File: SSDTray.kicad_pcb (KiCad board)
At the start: 2 copper layers, 216 x 80 mm, 22 parts, among them J1 SSD1, J10 SSD10, J11 SSD11, J12 SSD12, J13 SSD13, J14 SSD14, J15 SSD15, J16 SSD16, J17 SSD17, J18 SSD18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

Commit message: Remove autosave lock file and update active layer preset to 'All Layers'
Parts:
- turned J19 to 0 degrees
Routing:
- net /SSD3_TX+: track 0.00 -> 61.6 mm
- net /SSD3_TX-: track 0.00 -> 59.3 mm
- net /SSD1_TX-: track 0.00 -> 28.6 mm
- net /SSD1_TX+: track 0.00 -> 25.9 mm
- net /SSD2_TX-: track 0.00 -> 25.2 mm
- net /SSD2_TX+: track 0.00 -> 22.5 mm
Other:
- copper layers 2 -> 4

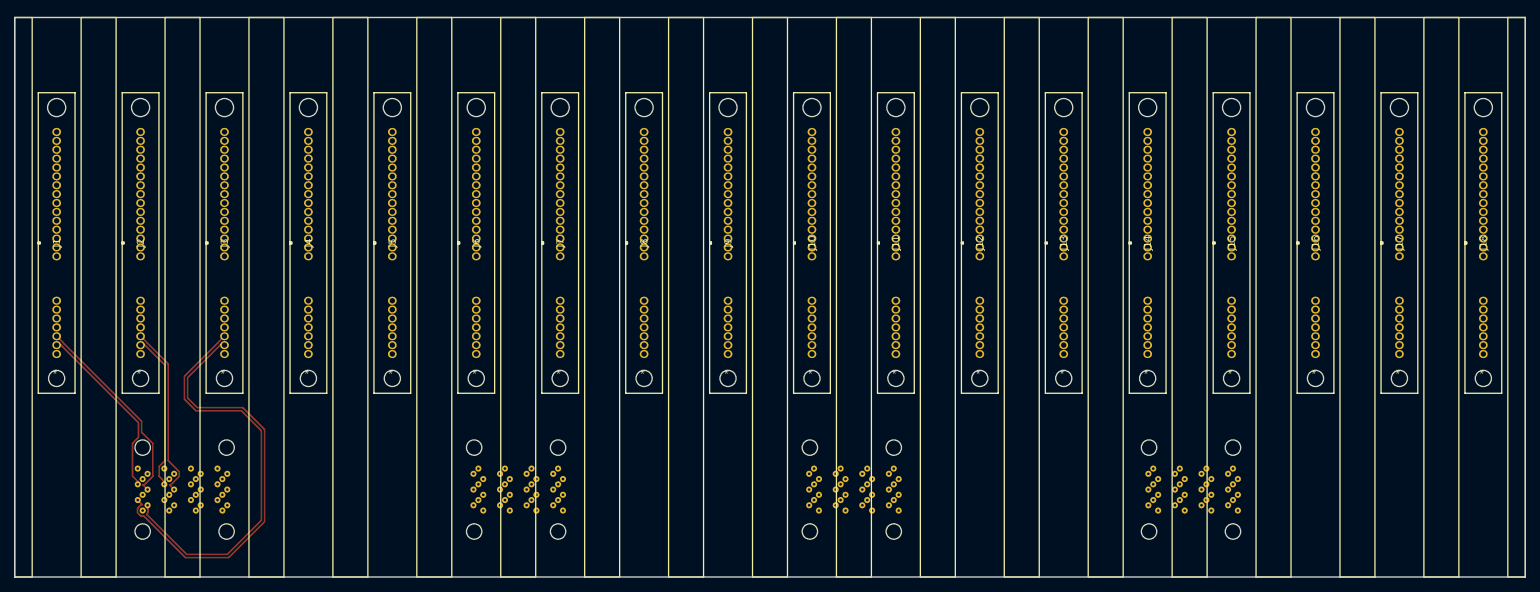
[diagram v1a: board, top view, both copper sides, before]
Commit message: Add Molex Connector footprint and symbol to libraries
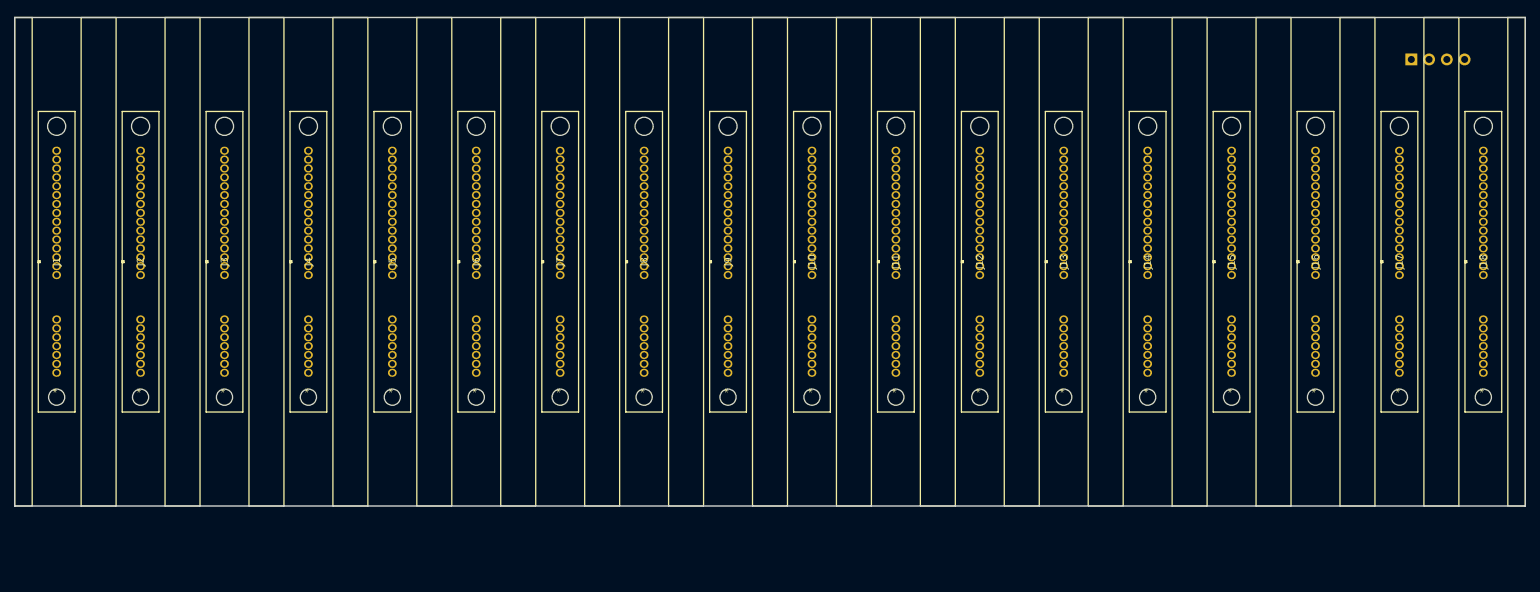
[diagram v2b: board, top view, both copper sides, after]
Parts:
- removed J19: SSD1-4, Mini SAS HD:TE_2227595-1
- removed J20: SSD5-8, Mini SAS HD:TE_2227595-1
- removed J21: SSD9-12, Mini SAS HD:TE_2227595-1
- removed J22: SSD13-16, Mini SAS HD:TE_2227595-1
- added J23: Conn_01x04, Connector_PinHeader_2.54mm:PinHeader_1x04_P2.54mm_Vertical, B.Cu at (227.7, 107.0)
- moved J1 2.68 mm to (34.0, 151.8)
- moved J10 2.68 mm to (142.0, 151.8)
- moved J11 2.68 mm to (154.0, 151.8)
- moved J12 2.68 mm to (166.0, 151.8)
- moved J13 2.68 mm to (178.0, 151.8)
- moved J14 2.68 mm to (190.0, 151.8)
- moved J15 2.68 mm to (202.0, 151.8)
- moved J16 2.68 mm to (214.0, 151.8)
- moved J17 2.68 mm to (226.0, 151.8)
- moved J18 2.68 mm to (238.0, 151.8)
- moved J2 2.68 mm to (46.0, 151.8)
- moved J3 2.68 mm to (58.0, 151.8)
- moved J4 2.68 mm to (70.0, 151.8)
- moved J5 2.68 mm to (82.0, 151.8)
- moved J6 2.68 mm to (94.0, 151.8)
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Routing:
- net /SSD3_TX+: track 61.6 -> 0.00 mm
- net /SSD3_TX-: track 59.3 -> 0.00 mm
- net /SSD1_TX-: track 28.6 -> 0.00 mm
- net /SSD1_TX+: track 25.9 -> 0.00 mm
- net /SSD2_TX-: track 25.2 -> 0.00 mm
- net /SSD2_TX+: track 22.5 -> 0.00 mm
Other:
- board size 216 x 80 mm -> 216 x 69.8 mm

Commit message: Add Mini SAS footprint and symbol to libraries; update design rules and dimensions in SSDTray.kicad_pro
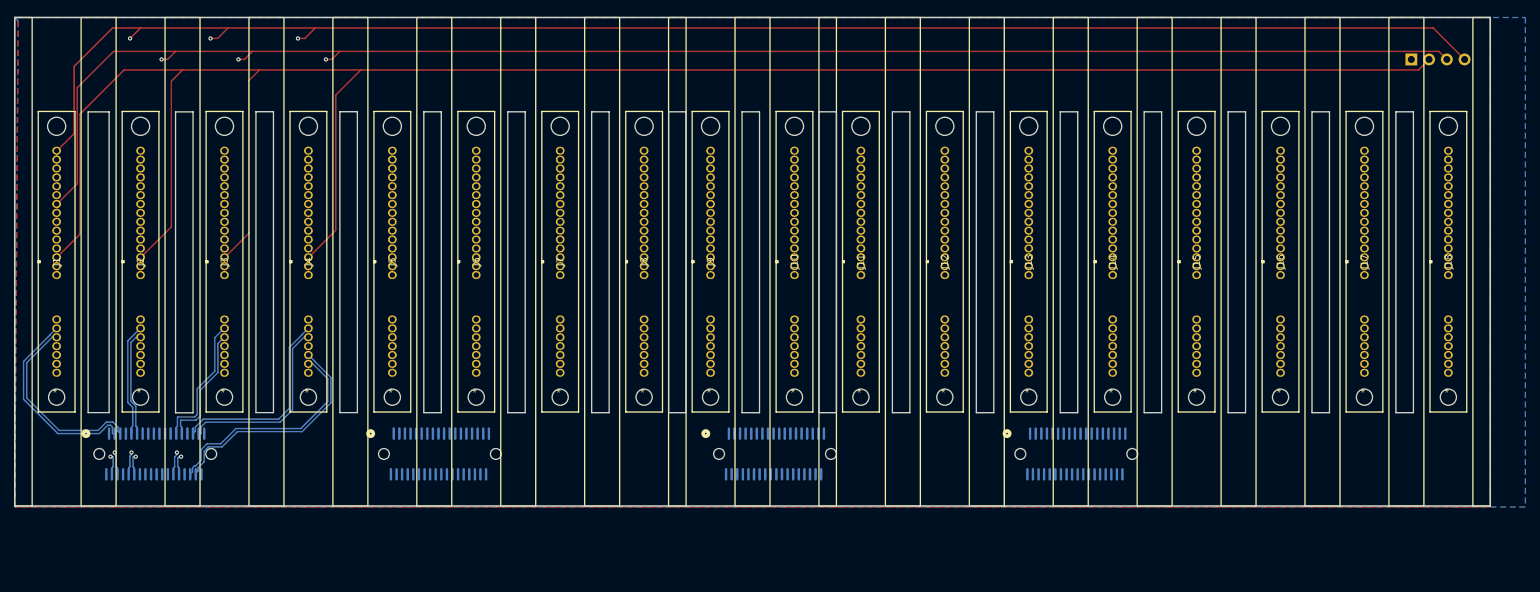
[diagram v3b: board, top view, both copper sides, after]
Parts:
- added J19: 1888020-4, Mini SAS:CONN36_1888020-4_TEC, B.Cu at (82.2, 160.5)
- added J20: 1888020-4, Mini SAS:CONN36_1888020-4_TEC, B.Cu at (41.5, 160.5)
- added J21: 1888020-4, Mini SAS:CONN36_1888020-4_TEC, B.Cu at (130.1, 160.5)
- added J22: 1888020-4, Mini SAS:CONN36_1888020-4_TEC, B.Cu at (173.2, 160.5)
- moved J11 5.00 mm to (149.0, 151.8)
- moved J12 5.00 mm to (161.0, 151.8)
- moved J13 5.00 mm to (173.0, 151.8)
- moved J14 5.00 mm to (185.0, 151.8)
- moved J15 5.00 mm to (197.0, 151.8)
- moved J16 5.00 mm to (209.0, 151.8)
- moved J17 5.00 mm to (221.0, 151.8)
- moved J18 5.00 mm to (233.0, 151.8)
- moved J10 2.50 mm to (139.5, 151.8)
- moved J9 2.50 mm to (127.5, 151.8)
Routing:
- net +3.3V: track 0.00 -> 318.8 mm
- net +5V: track 0.00 -> 299.1 mm, vias 0 -> 3
- net +12V: track 0.00 -> 284.9 mm, vias 0 -> 3
- net /SSD4_TX-: track 0.00 -> 33.0 mm
- net /SSD4_TX+: track 0.00 -> 32.1 mm
- net /SSD1_RX+: track 0.00 -> 28.7 mm
- net /SSD4_RX+: track 0.00 -> 28.2 mm
- net /SSD1_RX-: track 0.00 -> 27.7 mm
- net /SSD4_RX-: track 0.00 -> 27.1 mm
- net /SSD3_TX-: track 0.00 -> 21.9 mm, vias 0 -> 1
- net /SSD1_TX-: track 0.00 -> 20.8 mm, vias 0 -> 1
- net /SSD3_TX+: track 0.00 -> 20.7 mm, vias 0 -> 1
- net /SSD1_TX+: track 0.00 -> 19.6 mm, vias 0 -> 1
- net /SSD3_RX+: track 0.00 -> 19.4 mm
- net /SSD2_TX-: track 0.00 -> 19.3 mm, vias 0 -> 1
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- added copper zone on B.Cu, net GND
- added copper zone on F.Cu, net GND
- added copper zone on In2.Cu, net GND
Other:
- board size 216 x 69.8 mm -> 211 x 69.8 mm

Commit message: Limiting to 4 drives for testing
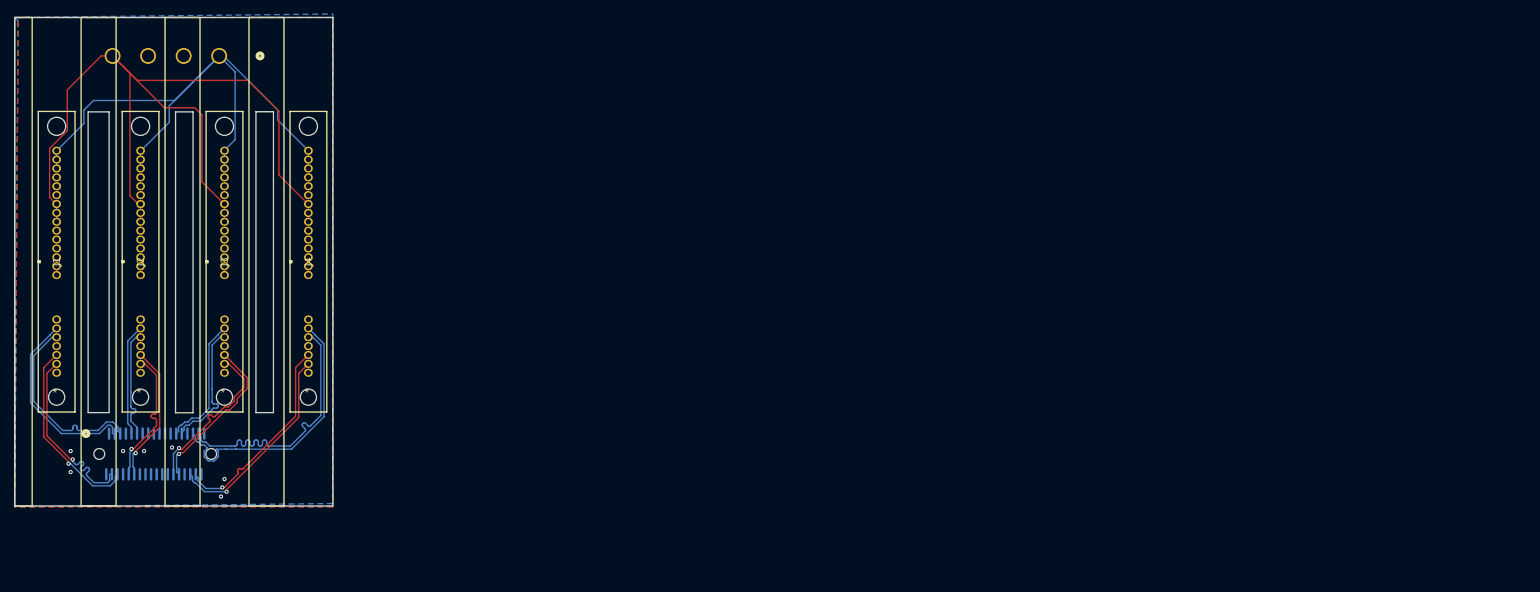
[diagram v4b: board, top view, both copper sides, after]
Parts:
- removed J10: SSD10, SSD Connector:CONN_877791001_MOL
- removed J11: SSD11, SSD Connector:CONN_877791001_MOL
- removed J12: SSD12, SSD Connector:CONN_877791001_MOL
- removed J13: SSD13, SSD Connector:CONN_877791001_MOL
- removed J14: SSD14, SSD Connector:CONN_877791001_MOL
- removed J15: SSD15, SSD Connector:CONN_877791001_MOL
- removed J16: SSD16, SSD Connector:CONN_877791001_MOL
- removed J17: SSD17, SSD Connector:CONN_877791001_MOL
- removed J18: SSD18, SSD Connector:CONN_877791001_MOL
- removed J19, J21, J22: 1888020-4, Mini SAS:CONN36_1888020-4_TEC
- removed J23: Conn_01x04, Connector_PinHeader_2.54mm:PinHeader_1x04_P2.54mm_Vertical
- removed the J5 at (82.0, 151.8)
- removed J6: SSD6, SSD Connector:CONN_877791001_MOL
- removed J7: SSD7, SSD Connector:CONN_877791001_MOL
- removed J8: SSD8, SSD Connector:CONN_877791001_MOL
- removed J9: SSD9, SSD Connector:CONN_877791001_MOL
- added U1: 350211-1, 4Pin ATX Molex:350211-1_TYC, B.Cu at (57.2, 106.5)
- renumbered J20 to J5
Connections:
- J1 pad P1: +3.3V -> unconnected-(J1-PadP1)
- J1 pad P2: +3.3V -> unconnected-(J1-PadP1)
- J1 pad P3: +3.3V -> unconnected-(J1-PadP1)
- J2 pad P1: +3.3V -> unconnected-(J2-PadP1)
- J2 pad P2: +3.3V -> unconnected-(J2-PadP1)
- J2 pad P3: +3.3V -> unconnected-(J2-PadP1)
- J3 pad P1: +3.3V -> unconnected-(J3-PadP1)
- J3 pad P2: +3.3V -> unconnected-(J3-PadP1)
- J3 pad P3: +3.3V -> unconnected-(J3-PadP1)
- J4 pad P1: +3.3V -> unconnected-(J4-PadP1)
- J4 pad P2: +3.3V -> unconnected-(J4-PadP1)
- J4 pad P3: +3.3V -> unconnected-(J4-PadP1)
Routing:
- net +3.3V: track 318.8 -> 0.00 mm
- net +12V: track 284.9 -> 92.7 mm, vias 3 -> 0
- net +5V: track 299.1 -> 129.8 mm, vias 3 -> 0
- net /SSD4_RX-: track 27.1 -> 39.1 mm
- net /SSD4_RX+: track 28.2 -> 39.3 mm
- net /SSD1_TX+: track 19.6 -> 27.3 mm
- net /SSD1_TX-: track 20.8 -> 27.1 mm
- net /SSD4_TX-: track 33.0 -> 29.7 mm, vias 0 -> 1
- net /SSD3_TX+: track 20.7 -> 23.4 mm
- net unconnected-(J4-PadP1): track 0.00 -> 2.54 mm
- net unconnected-(J3-PadP1): track 0.00 -> 2.54 mm
- net unconnected-(J2-PadP1): track 0.00 -> 2.54 mm
- net unconnected-(J1-PadP1): track 0.00 -> 2.54 mm
- net /SSD4_TX+: track 32.1 -> 29.9 mm, vias 0 -> 1
- net /SSD2_TX+: track 18.0 -> 20.0 mm
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- added copper zone on In1.Cu, net GND
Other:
- board size 211 x 69.8 mm -> 45.5 x 69.8 mm

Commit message: confused now
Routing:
- net +12V: track 92.7 -> 84.5 mm
- net +5V: track 129.8 -> 128.8 mm
